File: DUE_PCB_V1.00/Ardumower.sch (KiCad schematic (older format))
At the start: 54 parts, among them J1 9V IN, J10 Sonar_R, J11 Sonar_C, J12 Sonar_L, J13 P_Right, J14 Buzzer, J15 Button, J16 Button, J17 Button, J18 Button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

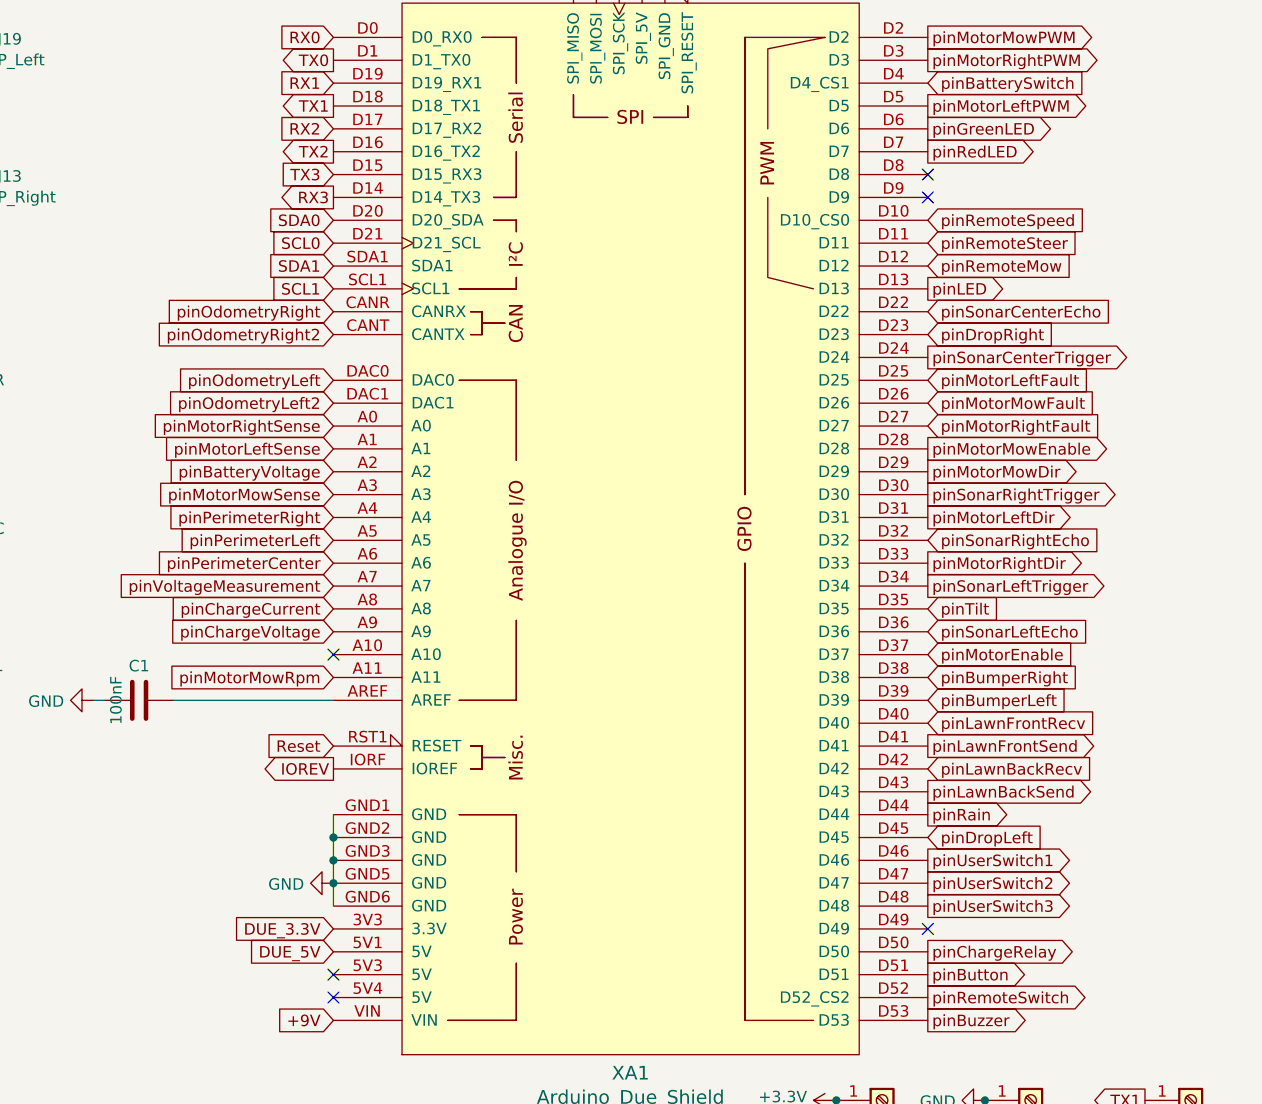
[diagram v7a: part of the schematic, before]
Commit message: Add ReservePins
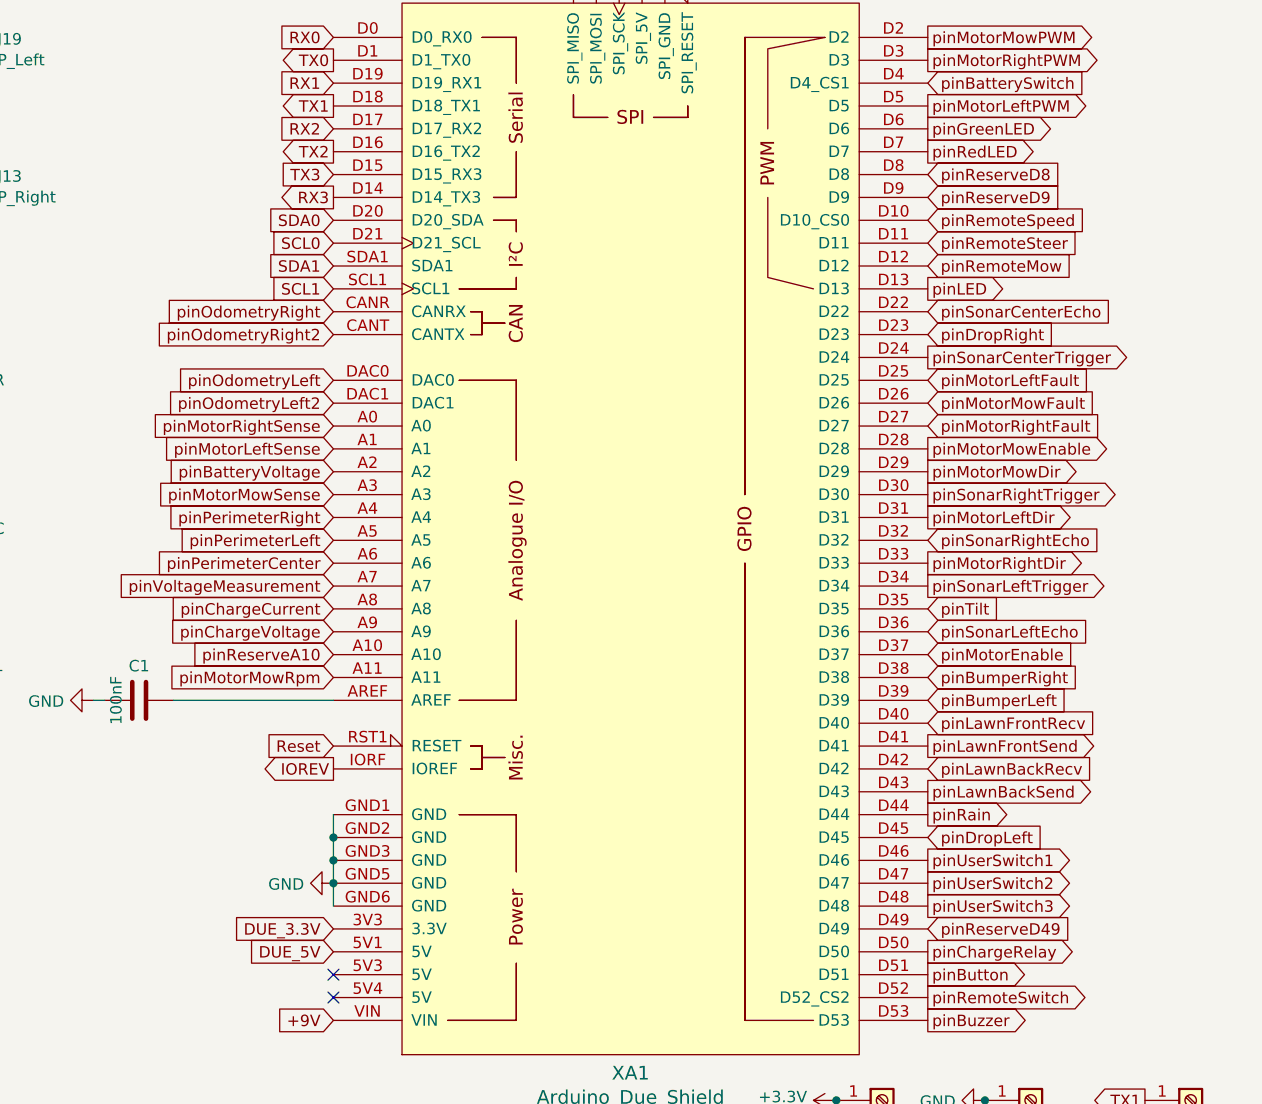
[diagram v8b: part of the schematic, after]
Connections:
- net pinReserveA10: now reaches XA1.A10
- net pinReserveD49: now reaches XA1.D49
- net pinReserveD8: now reaches XA1.D8
- net pinReserveD9: now reaches XA1.D9
- no-connect marks 6 -> 2
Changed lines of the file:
@@
 NoConn ~ 4850 5600
 NoConn ~ 4850 5700
-NoConn ~ 4850 4200
-NoConn ~ 7450 5400
-NoConn ~ 7450 2200
 $Comp
 L power:GND #PWR019
@@
 Text GLabel 7450 1500 2    50   Output ~ 0
 pinMotorMowPWM
-NoConn ~ 7450 2100
 Text GLabel 7450 3400 2    50   Output ~ 0
 pinMotorMowDir
@@
 	1    0    0    -1
 $EndComp
+Text GLabel 7450 2100 2    50   Input ~ 0
+pinReserveD8
+Text GLabel 7450 2200 2    50   Input ~ 0
+pinReserveD9
+Text GLabel 7450 5400 2    50   Input ~ 0
+pinReserveD49
+Text GLabel 4850 4200 0    50   Input ~ 0
+pinReserveA10
 $EndSCHEMATC
